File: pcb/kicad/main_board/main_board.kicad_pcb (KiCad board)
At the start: 2 copper layers, 131.2 x 78 mm, 91 parts, among them J1 Power, J10 OUT2, J2 IN1, J3 IN2, J4 B2B_A, J5 B2B_B, J6 LCD2WIRE, J7 DS18B20, J8 PROG, J9 OUT1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

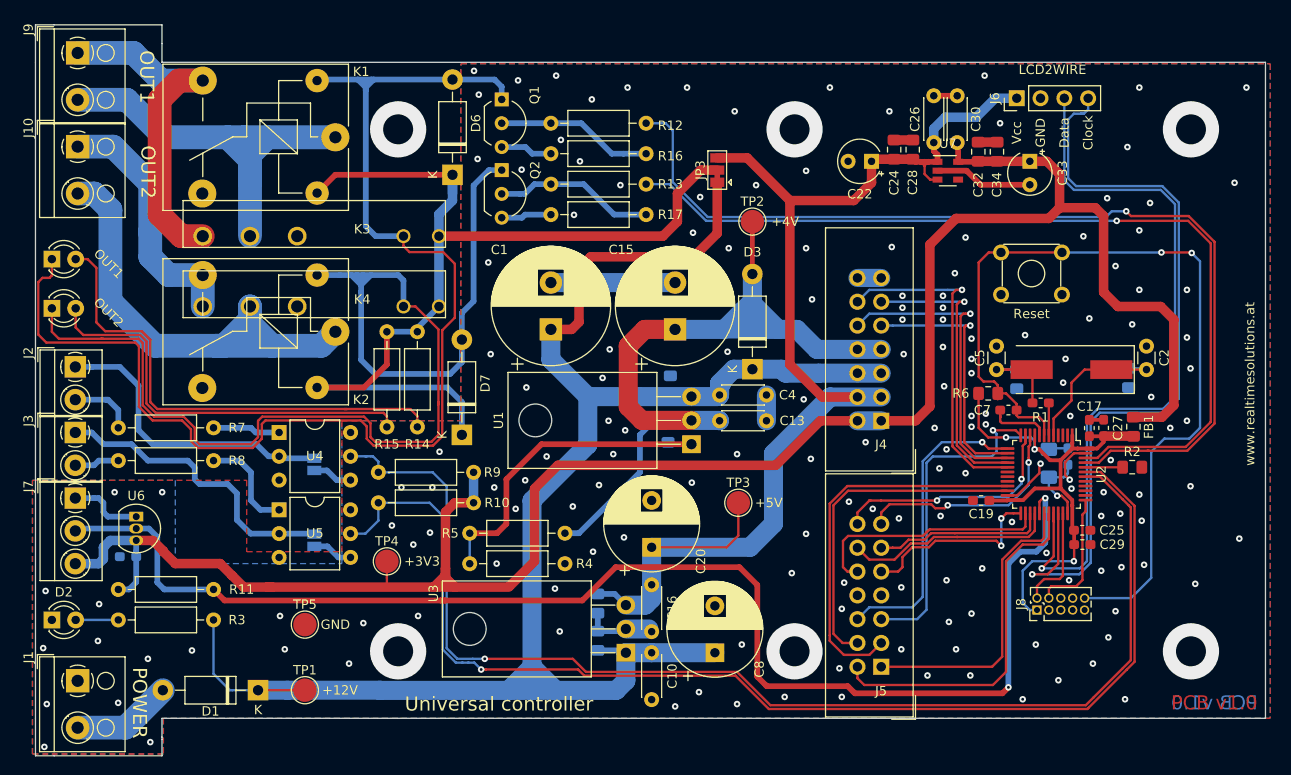
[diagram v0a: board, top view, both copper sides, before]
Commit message: Add main board PCB ver.1.1
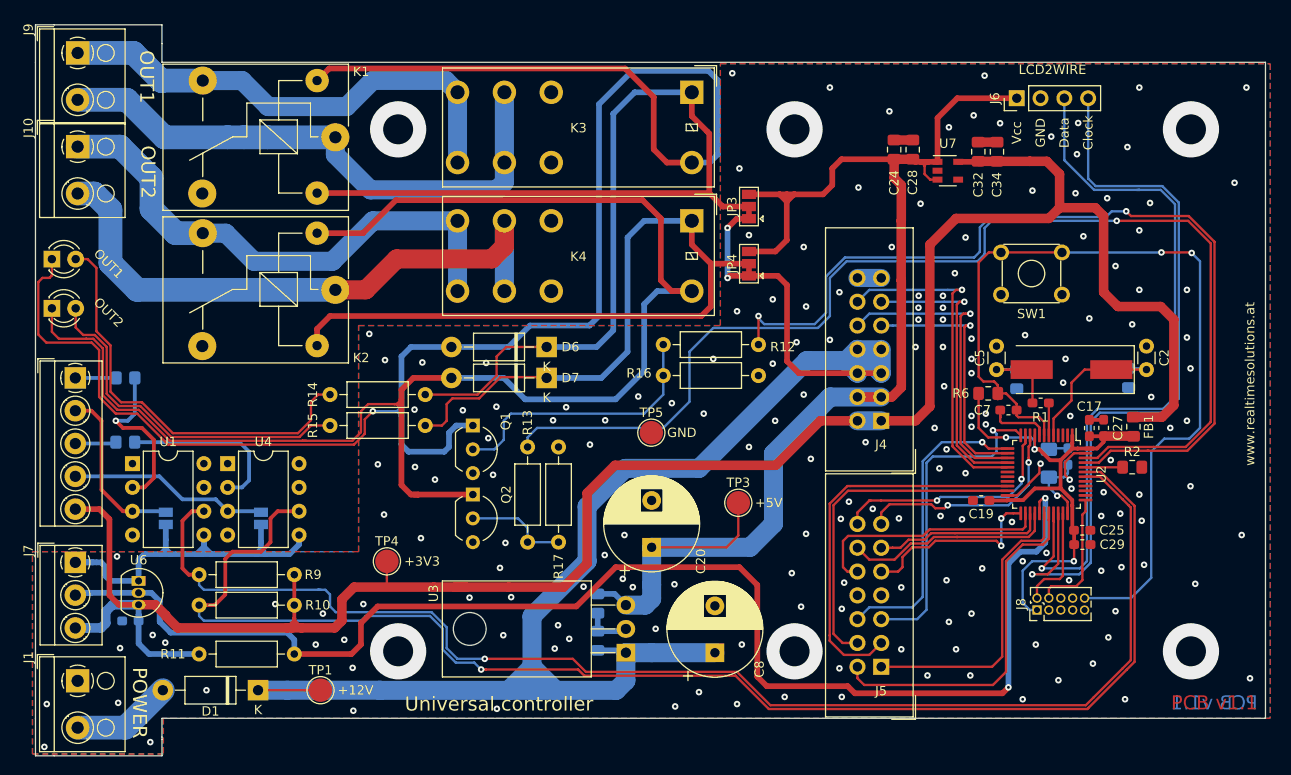
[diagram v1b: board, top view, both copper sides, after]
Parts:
- removed C1, C15: 1000uF, Capacitor_THT:CP_Radial_D12.5mm_P5.00mm
- removed C10, C13, C16, C26, C30, C4: 100nF, Capacitor_THT:C_Disc_D4.3mm_W1.9mm_P5.00mm
- removed C12, C6: 100nF*, Capacitor_SMD:C_0805_2012Metric_Pad1.15x1.40mm_HandSolder
- removed C22, C33: 10uF, Capacitor_THT:CP_Radial_Tantal_D4.5mm_P2.50mm
- removed D2: LED, LED_THT:LED_D3.0mm
- removed D3: 1N4007, Diode_THT:D_DO-41_SOD81_P10.16mm_Horizontal
- removed J3: IN2, TerminalBlock_MetzConnect:TerminalBlock_MetzConnect_Type059_RT06302HBWC_1x02_P3.50mm_Horizontal
- removed R3: 4K7, Resistor_THT:R_Axial_DIN0207_L6.3mm_D2.5mm_P10.16mm_Horizontal
- removed R4: 470, Resistor_THT:R_Axial_DIN0207_L6.3mm_D2.5mm_P10.16mm_Horizontal
- removed R5: 220, Resistor_THT:R_Axial_DIN0207_L6.3mm_D2.5mm_P10.16mm_Horizontal
- removed TP2: +4V, TestPoint:TestPoint_Pad_D2.5mm
- removed U5: CNY17-2, Package_DIP:DIP-6_W7.62mm
- added JP4: Relay_Power, Jumper:SolderJumper-3_P1.3mm_Bridged12_Pad1.0x1.5mm, F.Cu at (56.1, -48.5)
- C11, C18, C28, C32: value 100nF* -> 100nF
- C24, C34: value 10uF* -> 10uF
- J2: value IN1 -> Inputs; footprint TerminalBlock_MetzConnect:TerminalBlock_MetzConnect_Type059_RT06302HBWC_1x02_P3.50mm_Horizontal -> TerminalBlock_MetzConnect:TerminalBlock_MetzConnect_Type059_RT06305HBWC_1x05_P3.50mm_Horizontal
- K3, K4: value FTR-LYCA -> G2RL; footprint Relay_FTR:FTR-LYCA -> Relay_THT:Relay_DPDT_Omron_G2RL
- R7, R8: footprint Resistor_THT:R_Axial_DIN0207_L6.3mm_D2.5mm_P10.16mm_Horizontal -> Resistor_SMD:R_0805_2012Metric_Pad1.20x1.40mm_HandSolder; moved to B.Cu
- U1: value LM317 -> 6N135; footprint Package_TO_SOT_THT:TO-220-3_Horizontal_TabDown -> Package_DIP:DIP-8_W7.62mm
- U4: value CNY17-2 -> 6N135; footprint Package_DIP:DIP-6_W7.62mm -> Package_DIP:DIP-8_W7.62mm
- moved U1 59.7 mm to (-9.65, -27.2), turned to 0 degrees
- moved TP5 42.3 mm to (45.7, -30.5)
- moved R13 38.3 mm to (32.5, -18.8), turned to 90 degrees
- moved Q1 34.9 mm to (26.7, -31.2)
- moved Q2 34.8 mm to (26.7, -23.9)
- moved R16 32.4 mm to (57.1, -36.6), turned to 180 degrees
- moved K3 28.7 mm to (50.0, -66.8)
- moved K4 26.8 mm to (50.0, -53.1)
- moved R12 26.5 mm to (47.0, -39.9)
- moved R17 24.8 mm to (35.8, -29.0), turned to 270 degrees
- moved R10 22.0 mm to (7.62, -12.1)
- moved R9 22.0 mm to (7.62, -15.3)
- moved D6 20.9 mm to (34.5, -39.6), turned to 180 degrees
- moved JP1 16.9 mm to (-6.10, -21.3)
- moved R11 11.0 mm to (7.62, -6.86)
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- renumbered Reset to SW1
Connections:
- D6 pad 1: RLY_PWR -> RLY1_PWR
- D7 pad 1: RLY_PWR -> RLY2_PWR
- J4 pad 7: +4V -> +12V
- J4 pad 8: +4V -> +12V
- JP1 pad 1: Net-(J2-Pad1) -> Net-(J2-Pad2)
- JP2 pad 1: Net-(J3-Pad1) -> Net-(J2-Pad4)
- JP3 pad 2: RLY_PWR -> RLY1_PWR
- K1 pad 5: RLY_PWR -> RLY1_PWR
- K2 pad 5: RLY_PWR -> RLY2_PWR
- K3 pad 1: RLY_PWR -> RLY1_PWR
- K3 pad 2: Net-(D4-Pad1) -> Net-(K3-Pad2)
- K3 pad 3: Net-(K3-Pad3) -> Net-(J9-Pad2)
- K3 pad 4: Net-(J9-Pad2) -> Net-(J9-Pad1)
- K4 pad 1: RLY_PWR -> RLY2_PWR
- K4 pad 2: Net-(D5-Pad1) -> Net-(K4-Pad2)
- K4 pad 3: Net-(K4-Pad3) -> Net-(J10-Pad2)
- K4 pad 4: Net-(J10-Pad2) -> Net-(J10-Pad1)
- R14 pad 1: RLY_PWR -> RLY1_PWR
- R15 pad 1: RLY_PWR -> RLY2_PWR
- R7 pad 2: Net-(J2-Pad2) -> Net-(J2-Pad1)
- R8 pad 2: Net-(J3-Pad2) -> Net-(J2-Pad3)
- U1 pad 2: +4V -> Net-(R7-Pad1)
- U1 pad 3: +12V -> Net-(J2-Pad2)
- U4 pad 1: Net-(R7-Pad1) -> Net-(U4-Pad1)
- U4 pad 2: Net-(J2-Pad1) -> Net-(R8-Pad1)
- U4 pad 3: Net-(U4-Pad3) -> Net-(J2-Pad4)
- U4 pad 4: GND -> Net-(U4-Pad4)
- U4 pad 5: IN1 -> GND
- U4 pad 6: Net-(U4-Pad6) -> IN2
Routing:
- net RLY1_PWR: track 0.00 -> 114.7 mm
- net RLY_PWR: track 105.5 -> 0.00 mm
- net RLY2_PWR: track 0.00 -> 104.6 mm
- net +4V: track 94.6 -> 0.00 mm
- net Net-(D4-Pad1): track 137.1 -> 198.2 mm, vias 0 -> 1
- net Net-(U1-Pad1): track 33.6 -> 0.00 mm
- net Net-(J3-Pad1): track 32.4 -> 0.00 mm
- net Net-(J10-Pad1): track 27.2 -> 56.8 mm
- net OUT2: track 96.9 -> 125.9 mm
- net Net-(J2-Pad1): track 32.3 -> 4.35 mm
- net Net-(D5-Pad1): track 135.1 -> 162.0 mm
- net +12V: track 199.2 -> 176.5 mm, vias 0 -> 2
- net IN2: track 129.1 -> 150.8 mm
- net Net-(J2-Pad4): track 0.00 -> 21.4 mm
- net GND: track 98.0 -> 83.7 mm, vias 169 -> 183
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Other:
- board text added: "PCB v1.1"
- board text removed: "PCB v1.0"
